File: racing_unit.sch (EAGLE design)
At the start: 55 parts, among them IC1 78L05Z, IC2 78L05Z, IC3 78L05Z, IC4 78L05Z, J1 J10MM, J2 J10MM, J3 J5MM, J4 J5MM, J5 J7MM, J7 J5MM, J8 J5MM, J9 J5MM, Q1 BDX54C, Q2 BDX54C, Q3 BDX54C, Q4 BDX54C

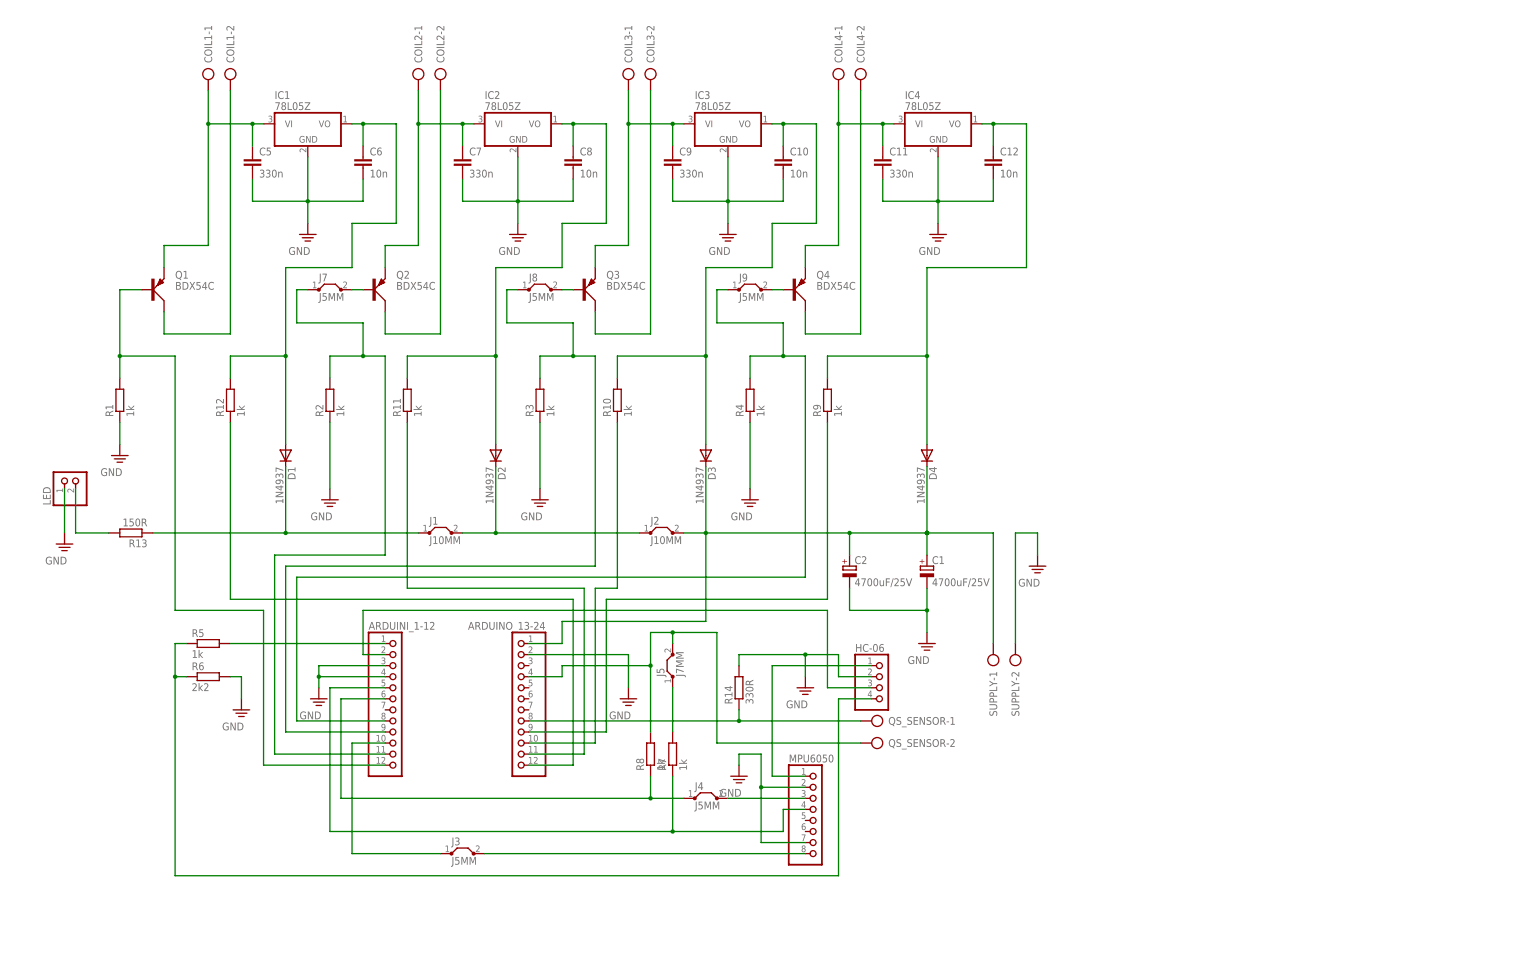
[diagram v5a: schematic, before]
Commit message: changed design to SMD
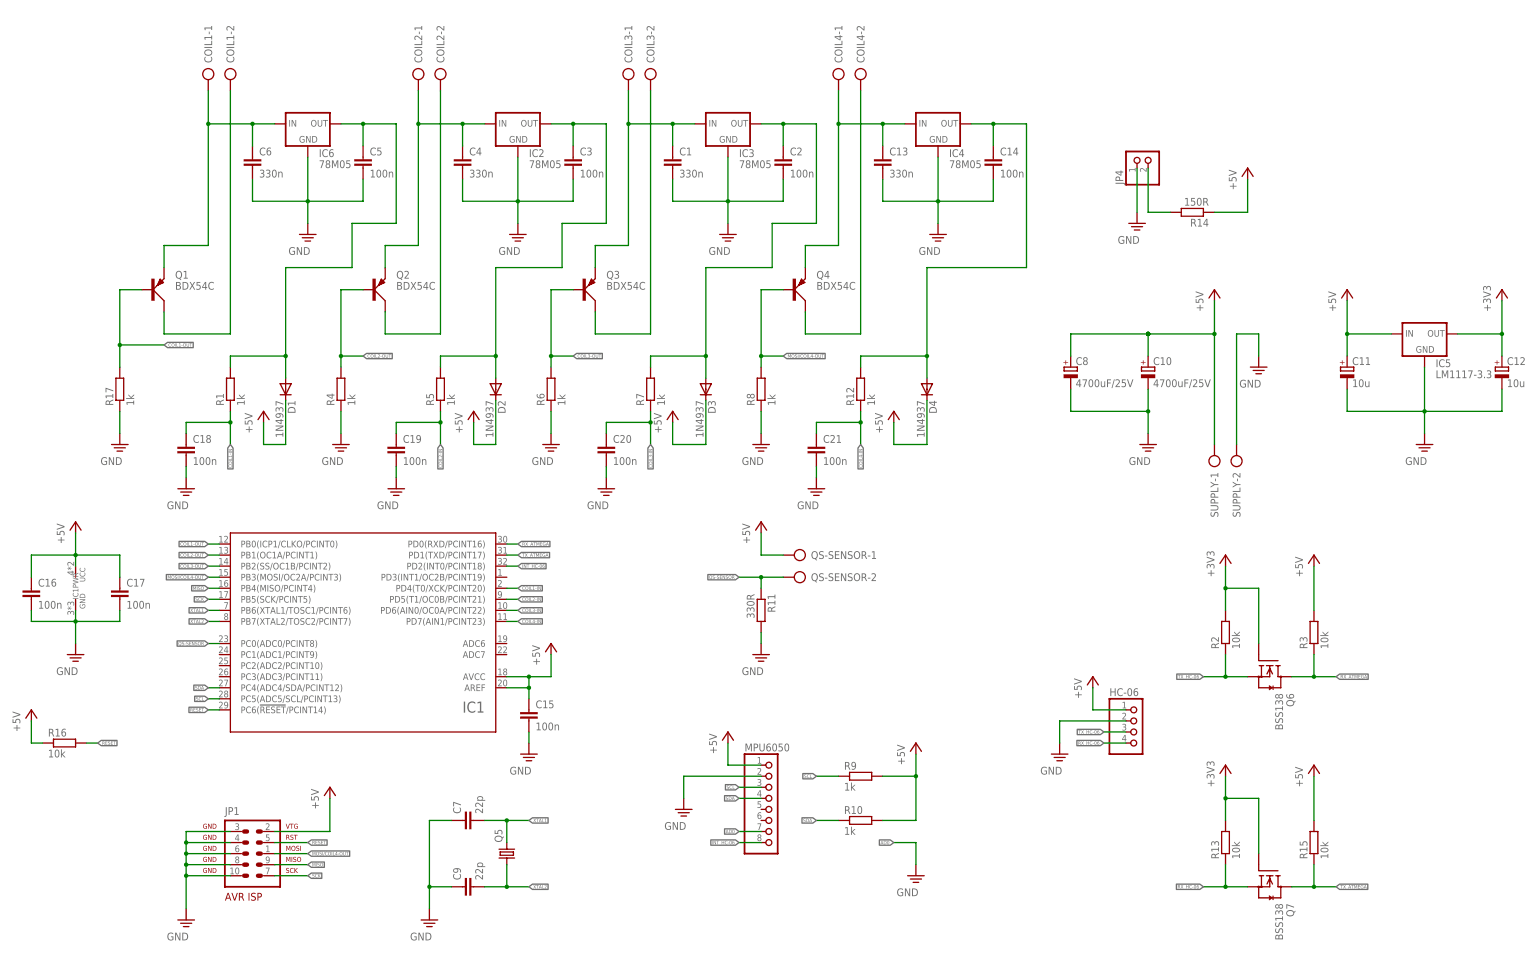
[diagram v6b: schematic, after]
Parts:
- removed ARDUINI_1-12, ARDUINO_13-24: (no value), pinhead:PINHD-1X12
- removed J1, J2: J10MM, jumper:J10MM
- removed J3, J4, J7, J8, J9: J5MM, jumper:J5MM
- removed J5: J7MM, jumper:J7MM
- removed LED: (no value), pinhead:PINHD-1X2
- removed QS_SENSOR: (no value), con-ptr500:AK500/2
- added C13, C4: 330n, rcl:C-EUC0805
- added C14, C15, C16, C17, C18, C19, C20, C21, C3: 100n, rcl:C-EUC0805
- added IC5: LM1117-3.3, v-reg-2:LM1117
- added IC6: 78M05, v-reg-2:LM1117TO252
- added JP1: AVR-ISP-10ML, atmel-1:AVR-ISP-10ML
- added JP4: (no value), pinhead:PINHD-1X2
- added Q5: (no value), crystal:CRYSTALHC49S
- added Q6, Q7: BSS138, m-pad-2.1:BSS138
- added QS-SENSOR: (no value), con-ptr500:AK500/2
- added R15, R16: 10k, rcl:R-EU_M0805
- added R17: 1k, rcl:R-EU_M0805
- C1: value 4700uF/25V -> 330n; device rcl:CPOL-EUE7.5-16 -> rcl:C-EUC0805
- C10, C8: value 10n -> 4700uF/25V; device rcl:C-EU050-024X044 -> rcl:CPOL-EUE7.5-16
- C11: value 330n -> 10u; device rcl:C-EU050-024X044 -> rcl:CPOL-EUA/3216-18R
- C12: value 10n -> 10u; device rcl:C-EU050-024X044 -> rcl:CPOL-EUA/3216-18R
- C2: value 4700uF/25V -> 100n; device rcl:CPOL-EUE7.5-16 -> rcl:C-EUC0805
- C5: value 330n -> 100n; device rcl:C-EU050-024X044 -> rcl:C-EUC0805
- C6: value 10n -> 330n; device rcl:C-EU050-024X044 -> rcl:C-EUC0805
- C7, C9: value 330n -> 22p; device rcl:C-EU050-024X044 -> rcl:C-EUC0805
- IC1: value 78L05Z -> (none); device linear:78L05Z -> atmel_tiny24-44-84tiny48-88mega48-88-168-328:ATMEGA48/88/168/328-AU
- IC2, IC3, IC4: value 78L05Z -> 78M05; device linear:78L05Z -> v-reg-2:LM1117TO252
- R1, R10, R12, R4, R5, R7, R8, R9: device resistor:R-EU_0204/5 -> rcl:R-EU_M0805
- R11: value 1k -> 330R
- R13: value 150R -> 10k; device resistor:R-EU_0204/5 -> rcl:R-EU_M0805
- R14: value 330R -> 150R
- R2, R3: value 1k -> 10k; device resistor:R-EU_0204/5 -> rcl:R-EU_M0805
- R6: value 2k2 -> 1k; device resistor:R-EU_0204/5 -> rcl:R-EU_M0805
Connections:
- removed net N$16: ARDUINO_13-24.8, QS_SENSOR-1.KL, R14.1
- removed net N$18: ARDUINO_13-24.4, J5.2, QS_SENSOR-2.KL, R8.2
- removed net N$19: ARDUINO_13-24.1, C1.+, C2.+, D3.C, D4.C, J2.2, SUPPLY-1.KL
- removed net N$20: ARDUINI_1-12.10, J3.1
- removed net N$22: ARDUINI_1-12.1, R5.2
- removed net N$23: ARDUINO_13-24.12, R12.1
- removed net N$24: ARDUINO_13-24.11, R11.1
- removed net N$25: ARDUINO_13-24.10, R10.1
- removed net N$26: ARDUINO_13-24.9, R9.1
- removed net N$27: ARDUINI_1-12.6, J4.1, R8.1
- removed net N$28: ARDUINI_1-12.12, Q1.B, R1.2
- removed net N$29: J3.2, MPU6050.8
- removed net N$30: J7.2, Q2.B
- removed net N$31: ARDUINI_1-12.5, MPU6050.4, R7.1
- removed net N$32: HC-06.4, R5.1, R6.1
- removed net N$33: J4.2, MPU6050.3
- removed net N$34: HC-06.1, MPU6050.1
- removed net N$35: ARDUINI_1-12.11, J7.1, R2.2
- removed net N$36: J5.1, R7.2
- removed net N$37: J8.2, Q3.B
- removed net N$38: ARDUINI_1-12.9, J8.1, R3.2
- removed net N$40: J9.2, Q4.B
- removed net N$41: ARDUINI_1-12.8, J9.1, R4.2
- removed net N$6: ARDUINI_1-12.2, HC-06.3
- removed net N$7: D1.C, J1.1, R13.1
- removed net N$8: D2.C, J1.2, J2.1
- new net +3V3: C12.+, IC5.OUT, Q6.G, Q7.G, R13.2, R2.2
- new net +5V: C10.+, C11.+, C15.1, C16.1, C17.1, C8.+, D1.C, D2.C, D3.C, D4.C, HC-06.1, IC1IC.AREF, IC1IC.AVCC, IC1PWR.UCC, IC5.IN, JP1.2, MPU6050.1, QS-SENSOR-1.KL, R10.2, R14.1, R15.2, R16.1, R3.2, R9.2, SUPPLY-1.KL
- new net AD0: MPU6050.7
- new net COIL1-IN: C18.1, IC1IC.PD4(T0/XCK/PCINT20), R1.1
- new net COIL1-OUT: IC1IC.PB0(ICP1/CLKO/PCINT0), Q1.B, R17.2
- new net COIL2-IN: C19.1, IC1IC.PD5(T1/OC0B/PCINT21), R5.1
- new net COIL2-OUT: IC1IC.PB1(OC1A/PCINT1), Q2.B, R4.2
- new net COIL3-IN: C20.1, IC1IC.PD6(AIN0/OC0A/PCINT22), R7.1
- new net COIL3-OUT: IC1IC.PB2(SS/OC1B/PCINT2), Q3.B, R6.2
- new net COIL4-IN: C21.1, IC1IC.PD7(AIN1/PCINT23), R12.1
- new net INT_HC-06: IC1IC.PD2(INT0/PCINT18), MPU6050.8
- new net MISO: IC1IC.PB4(MISO/PCINT4), JP1.9
- new net MOSI/COIL4-OUT: IC1IC.PB3(MOSI/OC2A/PCINT3), JP1.1, Q4.B, R8.2
- new net PE: C15.2, C18.2, C19.2, C20.2, C21.2
- new net QS-SENSOR: IC1IC.PC0(ADC0/PCINT8), QS-SENSOR-2.KL, R11.1
- new net RESET: IC1IC.PC6(!RESET!/PCINT14), JP1.5, R16.2
- new net RX_ATMEGA: IC1IC.PD0(RXD/PCINT16), Q6.D, R3.1
- new net RX_HC-06: HC-06.4, Q7.S, R13.1
- new net SCK: IC1IC.PB5(SCK/PCINT5), JP1.7
- new net SCL: IC1IC.PC5(ADC5/SCL/PCINT13), MPU6050.3, R9.1
- new net SDA: IC1IC.PC4(ADC4/SDA/PCINT12), MPU6050.4, R10.1
- new net TX_ATMEGA: IC1IC.PD1(TXD/PCINT17), Q7.D, R15.1
- new net TX_HC-06: HC-06.3, Q6.S, R2.1
- new net XTAL1: C7.2, IC1IC.PB6(XTAL1/TOSC1/PCINT6), Q5.2
- new net XTAL2: C9.2, IC1IC.PB7(XTAL2/TOSC2/PCINT7), Q5.1
- net GND: now also C1.2, C10.-, C11.-, C12.-, C13.2, C14.2, C16.2, C17.2, C2.2, C3.2, C4.2, C7.1, C8.-, C9.1, IC1PWR.GND, IC5.GND, IC6.GND, JP1.10, JP1.3, JP1.4, JP1.6, JP1.8, JP4.1, R11.2, R17.1, R6.1, R8.1; no longer ARDUINI_1-12.3, ARDUINI_1-12.4, ARDUINO_13-24.2, C1.-, C10.2, C11.2, C12.2, C2.-, C7.2, C8.2, C9.2, IC1.GND, LED.1, MPU6050.7, R1.1, R14.2, R2.1, R3.1, R6.2
- net N$1: now also C6.1, IC6.IN; no longer C5.1, IC1.VI
- net N$13: now also JP4.2, R14.2; no longer LED.2, R13.2
- net N$14: now also C5.1, IC6.OUT, R1.2; no longer C6.1, IC1.VO, R12.2
- net N$15: now also C3.1, IC2.OUT, R5.2; no longer C8.1, IC2.VO, R11.2
- net N$17: now also C14.1, IC4.OUT, R12.2; no longer C12.1, IC4.VO, R9.2
- net N$2: now also C4.1, IC2.IN; no longer C7.1, IC2.VI
- net N$21: now also C2.1, IC3.OUT, R7.2; no longer C10.1, IC3.VO, R10.2
- net N$3: now also C1.1, IC3.IN; no longer C9.1, IC3.VI
- net N$4: now also C13.1, IC4.IN; no longer C11.1, IC4.VI
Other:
- moved on the sheet: C5, C6, C7, C9, D1, D2, D3, D4, HC-06, MPU6050, R1, R10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
